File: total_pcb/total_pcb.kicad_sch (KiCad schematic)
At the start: 139 parts, among them IC1 TSSP4038, IC10 TSSP4038, IC11 TSSP4038, IC12 TSSP4038, IC13 TSSP4038, IC14 TSSP4038, IC15 TSSP4038, IC16 TSSP4038, IC2 TSSP4038, IC3 TSSP4038, IC4 TSSP4038, IC5 TSSP4038, IC6 TSSP4038, IC7 TSSP4038, IC8 TSSP4038, IC9 TSSP4038, Q1 NPN, Q2 NPN, Q3 NPN, SW1 SW_DPST_x2, U2 openMV_M7_R2

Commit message: pcb
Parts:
- added D16, D17, D23, D24, D25, D26, D27, D28, D29: D, Diode_SMD:D_MELF-RM10_Universal_Handsoldering, symbol Library:D
- 10KΩ_1, 10KΩ_2, 10KΩ_3, 10KΩ_4, 10KΩ_5, 10KΩ_6, 10KΩ_7, 10KΩ_8, 220Ω_1, 220Ω_10, 220Ω_11, 220Ω_12, 220Ω_13, 220Ω_14, 220Ω_15, 220Ω_16, 220Ω_17, 220Ω_18, 220Ω_19, 220Ω_2, 220Ω_20, 220Ω_21, 220Ω_22, 220Ω_23, 220Ω_24, 220Ω_25, 220Ω_26, 220Ω_27, 220Ω_28, 220Ω_29, 220Ω_3, 220Ω_30, 220Ω_31, 220Ω_32, 220Ω_33, 220Ω_34, 220Ω_35, 220Ω_36, 220Ω_4, 220Ω_5, 220Ω_6, 220Ω_7, 220Ω_8, 220Ω_9, R17, R18, R19: footprint (none) -> Resistor_THT:R_Axial_DIN0207_L6.3mm_D2.5mm_P10.16mm_Horizontal; symbol Device:R_US -> Library:R_US
- 3V3_conv1: footprint cust_footpr:pololu_power_converter -> Library:pololu-U1V10F5; symbol cust_symbs:pololu_3.3V,_3.7A_Step-Down_Voltage_Regulator_D30V30F3 -> Library:pololu_3.3V,_3.7A_Step-Down_Voltage_Regulator_D30V30F3
- 5V_conv1: footprint cust_footpr:pololu_power_converter -> Library:pololu-U1V10F5; symbol cust_symbs:pololu_5V,_3.4A_Step-Down_Voltage_Regulator_D30V30F5 -> Library:pololu_5V,_3.4A_Step-Down_Voltage_Regulator_D30V30F5
- D1, D10, D11, D12, D13, D14, D15, D18, D19, D2, D20, D21, D22, D3, D4, D5, D6, D7, D8, D9: symbol Device:D -> Library:D
- DR1: footprint cust_footpr:TB9051FTG -> Library:TB9051FTG; symbol cust_symbs:TB9051FTG -> Library:TB9051FTG_1
- DR2: footprint cust_footpr:TB9051FTG -> Library:TB9051FTG; symbol cust_symbs:TB9051FTG -> Library:TB9051FTG_2
- DR3: footprint cust_footpr:TB9051FTG -> Library:TB9051FTG; symbol cust_symbs:TB9051FTG -> Library:TB9051FTG
- F1: symbol Device:Fuse -> Library:Fuse
- IC1, IC10, IC11, IC12, IC13, IC14, IC15, IC16, IC2, IC3, IC4, IC5, IC6, IC7, IC8, IC9: footprint KiCad:TSSP4038 -> irsens:TSSP4038; symbol TSSP4038:TSSP4038 -> Library:TSSP4038
- IR_controller1, IR_controller2: footprint (none) -> Seeed Studio XIAO Series Library:XIAO-SAMD21-RP2040-14P-2.54-21X17.8MM (Seeeduino XIAO); symbol Seeed_Studio_XIAO_Series:Seeed Studio XIAO SAMD21 -> Library:Seeed Studio XIAO SAMD21
- LED1, LED10, LED11, LED12, LED2, LED3, LED4, LED5, LED6, LED7, LED8, LED9: symbol Device:LED_KRGB -> Library:LED_KRGB
- M1, M2, M3: footprint cust_footpr:pololu_4.41 Metal Gearmotor 25Dx63L mm MP 12V with 48 CPR Encoder -> Connector_PinHeader_1.27mm:PinHeader_1x06_P1.27mm_Vertical; symbol cust_symbs:pololu_4.4{colon}1_Metal_Gearmotor_25Dx63L_mm_MP_12V_with_48_CPR_Encoder -> Library:pololu_4.4{colon}1_Metal_Gearmotor_25Dx63L_mm_MP_12V_with_48_CPR_Encoder
- PR1, PR2, PR3, PR4, PR5, PR6, PR7, PR8: symbol Sensor_Optical:A1050 -> Library:A1050
- Q1, Q2, Q3: symbol Simulation_SPICE:NPN -> Library:NPN
- R1, R10, R11, R12, R13, R14, R15, R16, R2, R3, R4, R5, R6, R7, R8, R9: symbol Device:R_US -> Library:R_US
- SW1: symbol Switch:SW_DPST_x2 -> Library:SW_DPST_x2
- U2: footprint custom:openmv_m7_r2 -> Library:openmv_m7_r2; symbol openmv_m7_r2:openMV_M7_R2 -> Library:openMV_M7_R2
- solenoid1: symbol PCM_Elektuur:Re -> Library:Re
- teensy1: footprint cust_footpr:TEENSY41 -> teensy.pretty-master:Teensy41; symbol teensy:Teensy4.1 -> Library:Teensy4.1
- xt1, xt2: symbol Device:Battery -> Library:Battery
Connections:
- net 12V: now also D25.1 (K)
- net 5V: now also D16.2 (A), D23.1 (K); no longer PR1.1, PR2.1, PR3.1, PR4.1, PR5.1, PR6.1, PR7.1, PR8.1, Q1.1 (C)
- net BLAUW: now also teensy1.38 (16_A2_RX4_SCL1)
- net GND: now also D17.1 (K), D24.2 (A), D26.2 (A); no longer 10KΩ_1.2, 10KΩ_2.2, 10KΩ_3.2, 10KΩ_4.2, 10KΩ_5.2, 10KΩ_6.2, 10KΩ_7.2, 10KΩ_8.2, LED1.1 (K), LED10.1 (K), LED11.1 (K), LED12.1 (K), LED2.1 (K), LED3.1 (K), LED4.1 (K), LED5.1 (K), LED6.1 (K), LED7.1 (K), LED8.1 (K), LED9.1 (K)
- net GROEN: now also teensy1.25 (33_MCLK2)
- net ROOD: now also teensy1.26 (34_RX8)
- net S: now also teensy1.39 (17_A3_TX4_SDA1)
- net pr1: now also teensy1.35 (13_SCK_LED)
- net pr2: now also teensy1.33 (41_A17)
- net pr3: now also teensy1.32 (40_A16)
- net pr4: now also teensy1.31 (39_MISO1_OUT1A)
- net pr5: now also teensy1.30 (38_CS1_IN1)
- net pr6: now also teensy1.29 (37_CS)
- net pr7: now also teensy1.28 (36_CS)
- net pr8: now also teensy1.27 (35_TX8)
- net at R1.2, R10.2, R11.2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: now also D28.1 (K); no longer D6.2 (A), D8.1 (K)
- net at IC1.2 (GND), IC10.2 (GND), IC11.2 (GND)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: now also D29.2 (A); no longer D2.1 (K), D3.1 (K), D5.1 (K), D9.2 (A), SW1.1 (A), U2.screw
- net at D11.2 (A), D13.1 (K), DR1.0 (screw)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: now also D26.1 (K), D27.2 (A); no longer DR1.2 (GND), DR2.2 (GND), DR3.2 (GND), M1.3 (GND), M2.3 (GND), M3.3 (GND)
- net at 3V3_conv1.4 (GND), 3V3_conv1.5 (GND), 5V_conv1.4 (GND)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: now also D24.1 (K)
- net at D14.1 (K), D18.2 (A), D20.2 (A)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: now also D23.2 (A)
- net at D12.2 (A), DR1.1 (VIN), DR2.1 (VIN)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: now also D25.2 (A)
- net at DR1.10 (ENB): now also teensy1.18 (26_A12_MOSI1)
- net at DR1.11 (PWM2): now also teensy1.17 (25_A11_RX6_SDA2)
- net at DR1.12 (PWM1): now also teensy1.16 (24_A10_TX6_SCL2)
- net at DR1.9 (EN): now also teensy1.19 (27_A13_SCK1)
- net at DR3.10 (ENB): now also teensy1.7 (5_IN2)
- net at DR3.11 (PWM2): now also teensy1.6 (4_BCLK2)
- net at DR3.12 (PWM1): now also teensy1.5 (3_LRCLK2)
- net at DR3.9 (EN): now also teensy1.8 (6_OUT1D)
- net at teensy1.11 (9_OUT1C): now also DR2.12 (PWM1)
- net at teensy1.12 (10_CS_MQSR): now also DR2.11 (PWM2)
- net at teensy1.13 (11_MOSI_CTX1): now also DR2.10 (ENB)
- net at teensy1.14 (12_MISO_MQSL): now also DR2.9 (EN)
- net at teensy1.20 (28_RX7): now also M1.5 (A_out)
- net at teensy1.21 (29_TX7): now also M2.6 (B_out)
- net at teensy1.22 (30_CRX3): now also M2.5 (A_out)
- net at teensy1.23 (31_CTX3): now also M3.6 (B_out)
- net at teensy1.24 (32_OUT1B): now also M3.5 (A_out)
- net at teensy1.45 (23_A9_CRX1_MCLK1): now also M1.6 (B_out)
- new net: D16.1 (K), PR1.1, PR2.1, PR3.1, PR4.1, PR5.1, PR6.1, PR7.1, PR8.1, Q1.1 (C)
- new net: D2.1 (K), D29.1 (K), D3.1 (K), D5.1 (K), D9.2 (A), SW1.1 (A), U2.screw
- new net: 10KΩ_1.2, 10KΩ_2.2, 10KΩ_3.2, 10KΩ_4.2, 10KΩ_5.2, 10KΩ_6.2, 10KΩ_7.2, 10KΩ_8.2, D17.2 (A), LED1.1 (K), LED10.1 (K), LED11.1 (K), LED12.1 (K), LED2.1 (K), LED3.1 (K), LED4.1 (K), LED5.1 (K), LED6.1 (K), LED7.1 (K), LED8.1 (K), LED9.1 (K)
- new net: D27.1 (K), DR1.2 (GND), DR2.2 (GND), DR3.2 (GND), M1.3 (GND), M2.3 (GND), M3.3 (GND)
- new net: D28.2 (A), D6.2 (A), D8.1 (K)
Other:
- note added: "LEGENDA"
- moved on the sheet: solenoid1

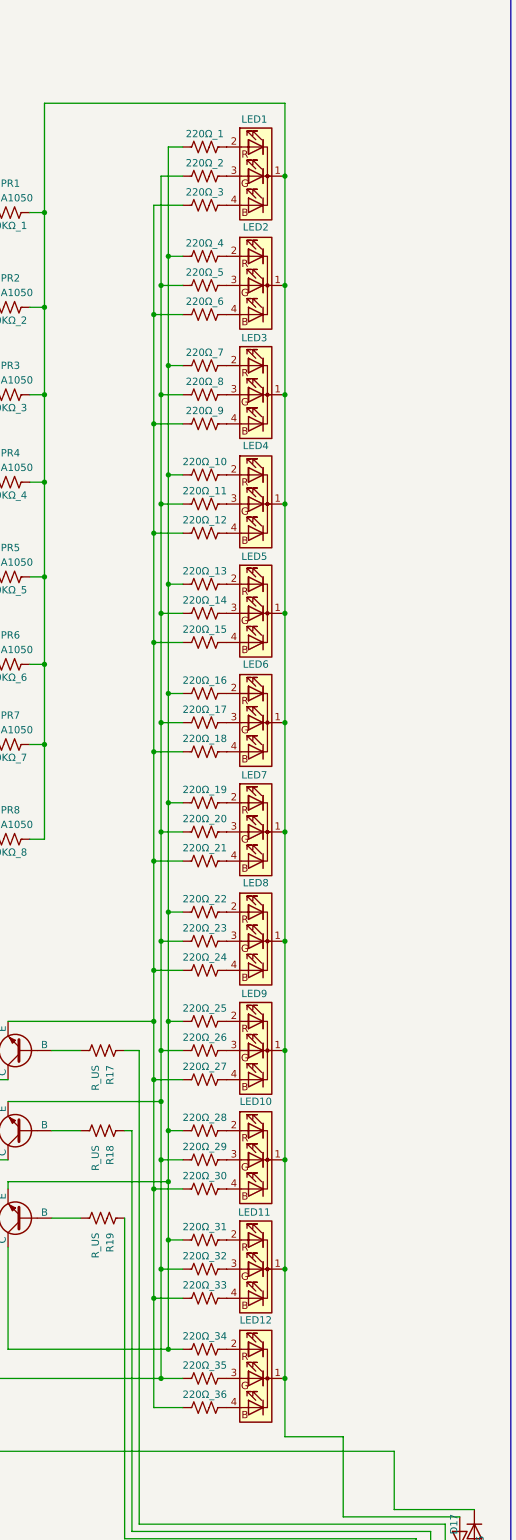
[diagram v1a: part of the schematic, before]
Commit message: update pcb led
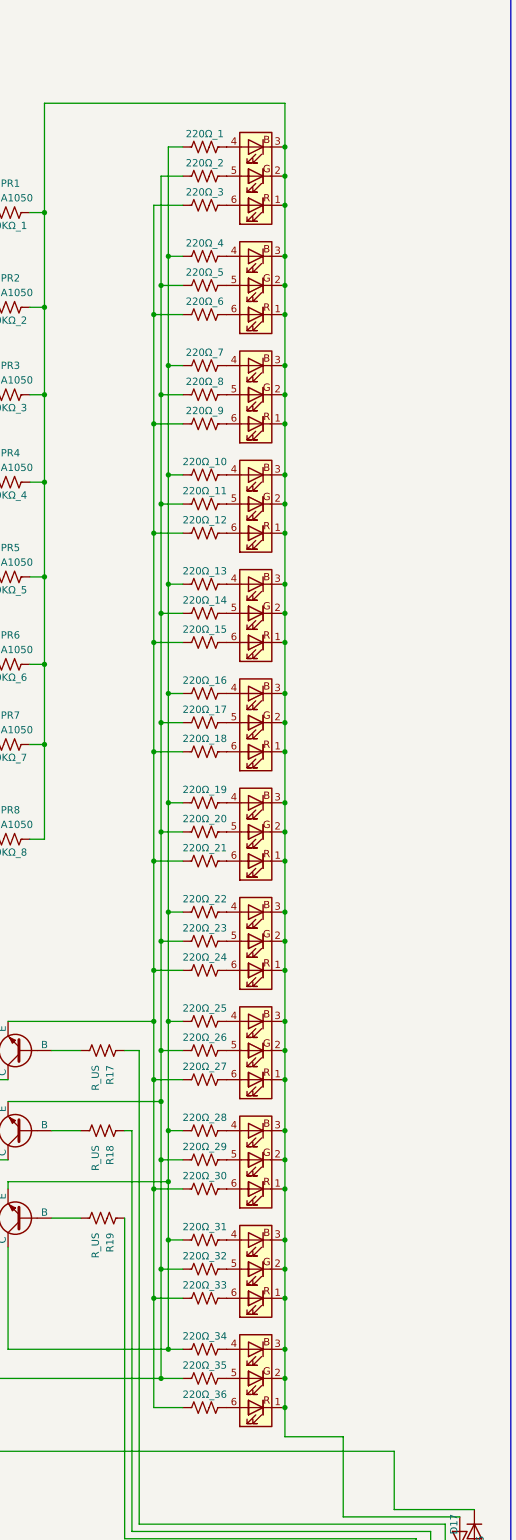
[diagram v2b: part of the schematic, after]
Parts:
- removed LED1, LED10, LED11, LED12, LED2, LED3, LED4, LED5, LED6, LED7, LED8, LED9: LED_KRGB, LED_THT:LED_D5.0mm-4_RGB_Wide_Pins, symbol Library:LED_KRGB
- added D30, D31, D32, D33, D34, D35, D36, D37, D38, D39, D40, D41: LED_RGB, symbol Device:LED_RGB
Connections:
- net at 220Ω_6.1: now also D31.6 (RA)
- net at 10KΩ_1.2, 10KΩ_2.2, 10KΩ_3.2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: now also D30.1 (RK), D30.2 (GK), D30.3 (BK), D31.1 (RK), D31.2 (GK), D31.3 (BK), D32.1 (RK), D32.2 (GK), D32.3 (BK), D33.1 (RK), D33.2 (GK), D33.3 (BK), D34.1 (RK), D34.2 (GK), D34.3 (BK), D35.1 (RK), D35.2 (GK), D35.3 (BK), D36.1 (RK), D36.2 (GK), D36.3 (BK), D37.1 (RK), D37.2 (GK), D37.3 (BK), D38.1 (RK), D38.2 (GK), D38.3 (BK), D39.1 (RK), D39.2 (GK), D39.3 (BK), D40.1 (RK), D40.2 (GK), D40.3 (BK), D41.1 (RK), D41.2 (GK), D41.3 (BK)
- net at 220Ω_18.1: now also D35.6 (RA)
- net at 220Ω_13.1: now also D34.4 (BA)
- net at 220Ω_31.1: now also D40.4 (BA)
- net at 220Ω_20.1: now also D36.5 (GA)
- net at 220Ω_2.1: now also D30.5 (GA)
- net at 220Ω_30.1: now also D39.6 (RA)
- net at 220Ω_24.1: now also D37.6 (RA)
- net at 220Ω_22.1: now also D37.4 (BA)
- net at 220Ω_17.1: now also D35.5 (GA)
- net at 220Ω_4.1: now also D31.4 (BA)
- net at 220Ω_5.1: now also D31.5 (GA)
- net at 220Ω_8.1: now also D32.5 (GA)
- net at 220Ω_16.1: now also D35.4 (BA)
- net at 220Ω_12.1: now also D33.6 (RA)
- net at 220Ω_1.1: now also D30.4 (BA)
- net at 220Ω_3.1: now also D30.6 (RA)
- net at 220Ω_14.1: now also D34.5 (GA)
- net at 220Ω_15.1: now also D34.6 (RA)
- net at 220Ω_32.1: now also D40.5 (GA)
- net at 220Ω_25.1: now also D38.4 (BA)
- net at 220Ω_26.1: now also D38.5 (GA)
- net at 220Ω_19.1: now also D36.4 (BA)
- net at 220Ω_23.1: now also D37.5 (GA)
- net at 220Ω_27.1: now also D38.6 (RA)
- net at 220Ω_28.1: now also D39.4 (BA)
- net at 220Ω_34.1: now also D41.4 (BA)
- net at 220Ω_35.1: now also D41.5 (GA)
- net at 220Ω_11.1: now also D33.5 (GA)
- net at 220Ω_36.1: now also D41.6 (RA)
- net at 220Ω_29.1: now also D39.5 (GA)
- net at 220Ω_10.1: now also D33.4 (BA)
- net at 220Ω_21.1: now also D36.6 (RA)
- net at 220Ω_33.1: now also D40.6 (RA)
- net at 220Ω_9.1: now also D32.6 (RA)
- net at 220Ω_7.1: now also D32.4 (BA)
